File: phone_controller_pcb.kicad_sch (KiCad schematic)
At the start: 17 parts, among them J1 USB_C_Receptacle_USB2.0_14P, J3 Conn_01x05_Pin, J4 Conn_01x05_Pin, J5 Conn_01x05_Pin, SW1 SW_SPDT, U1 nRF52840, U2 USBLC6-2P6, Y1 ECS-320-8-37B-CKY-TR, Y2 ABS05-32.768KHZ-9-T

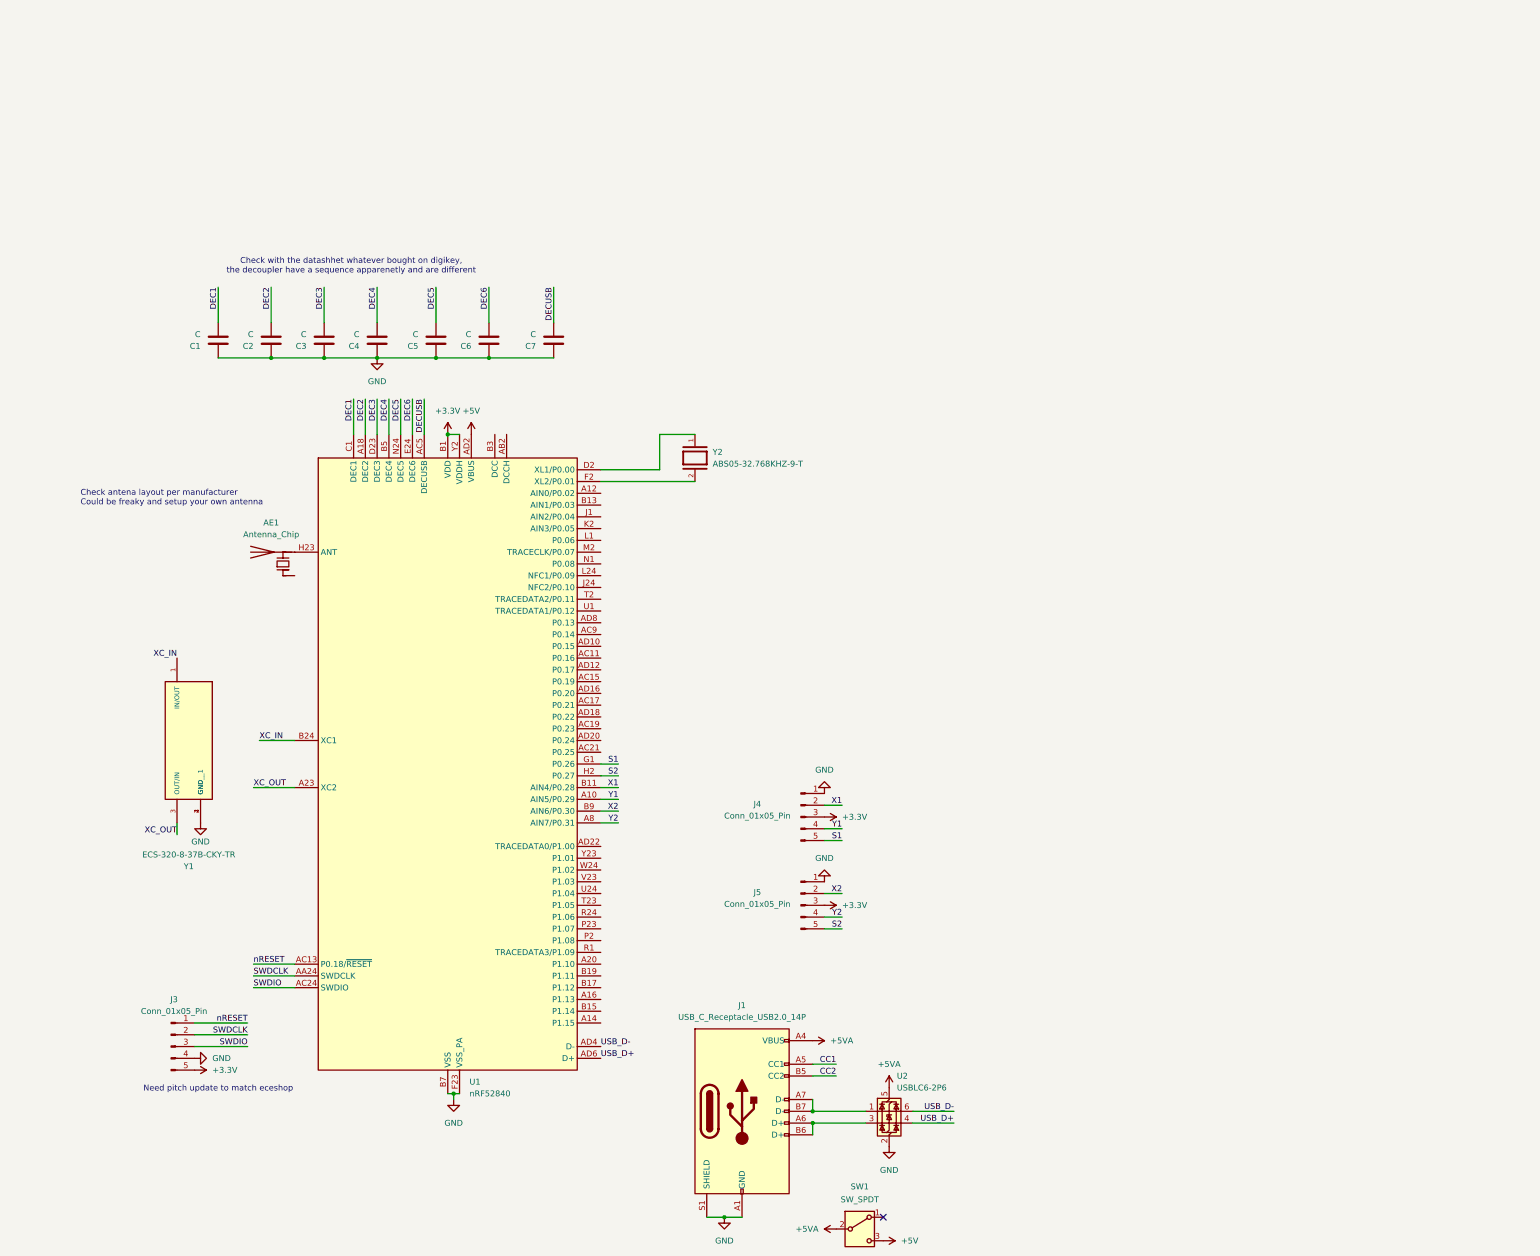
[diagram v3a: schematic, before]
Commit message: Added 3d model; update capacitor values
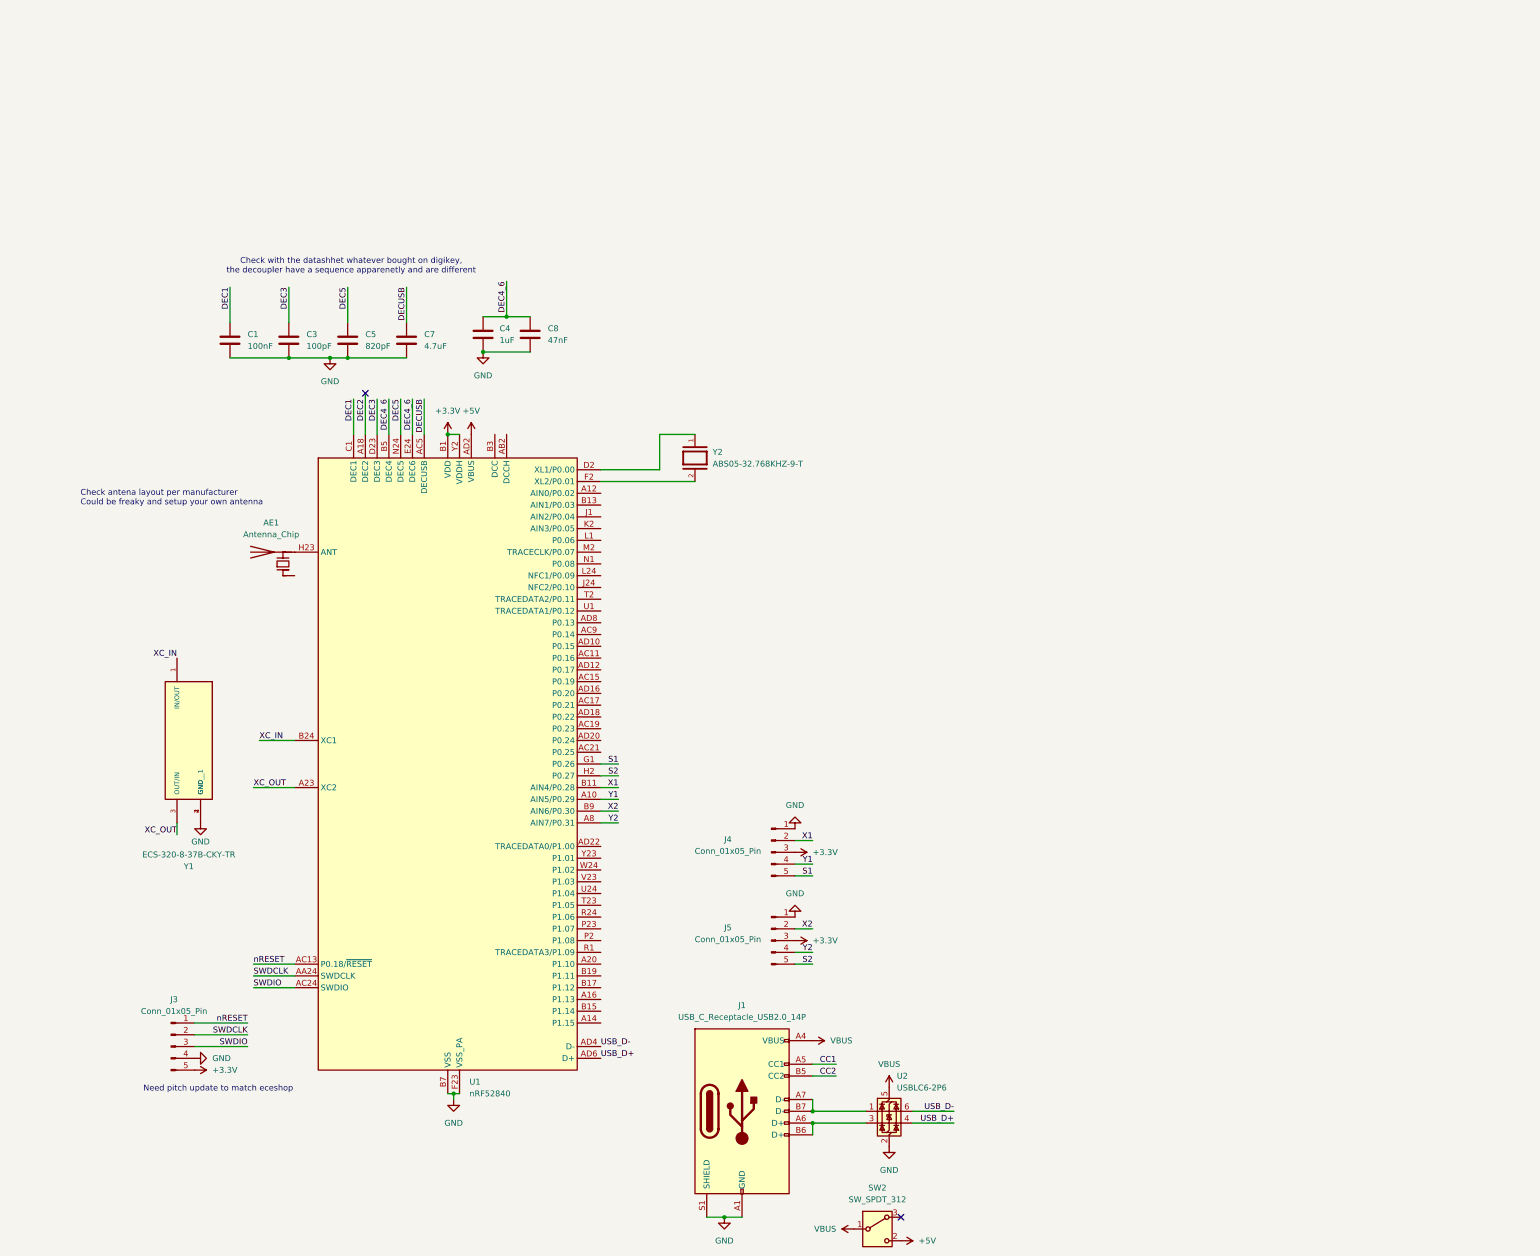
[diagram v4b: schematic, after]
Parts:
- removed C2, C6: C, Capacitor_SMD:C_0805_2012Metric, symbol Device:C
- removed SW1: SW_SPDT, symbol Switch:SW_SPDT
- added C8: 47nF, Capacitor_SMD:C_0805_2012Metric, symbol Device:C
- added SW2: SW_SPDT_312, footprints:OS102011MA1QN1_CNK, symbol Switch:SW_SPDT_312
- C1: value C -> 100nF
- C3: value C -> 100pF
- C4: value C -> 1uF
- C5: value C -> 820pF
- C7: value C -> 4.7uF
- J4, J5: footprint Connector_PinHeader_1.00mm:PinHeader_1x05_P1.00mm_Vertical -> 59453_052110ECHLF:AMPHENOL_59453-052110ECHLF; Digikey (none) -> https://www.digikey.com/en/products/detail/amphenol-icc-fci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
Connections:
- net DEC6 is gone; now on net DEC4_6: U1.E24 (DEC6)
- net +5V: now also SW2.2 (C)
- net GND: now also C8.2
- net +5VA renamed VBUS
- net VBUS: now also SW2.1 (B)
- net DEC4 renamed DEC4_6
- net DEC4_6: now also C8.1
- no-connect marks 1 -> 2
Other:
- moved on the sheet: C1, C3, C5, C7, J4, J5

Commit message: Added antenna setup; Added separator; Rounding out power capacitor
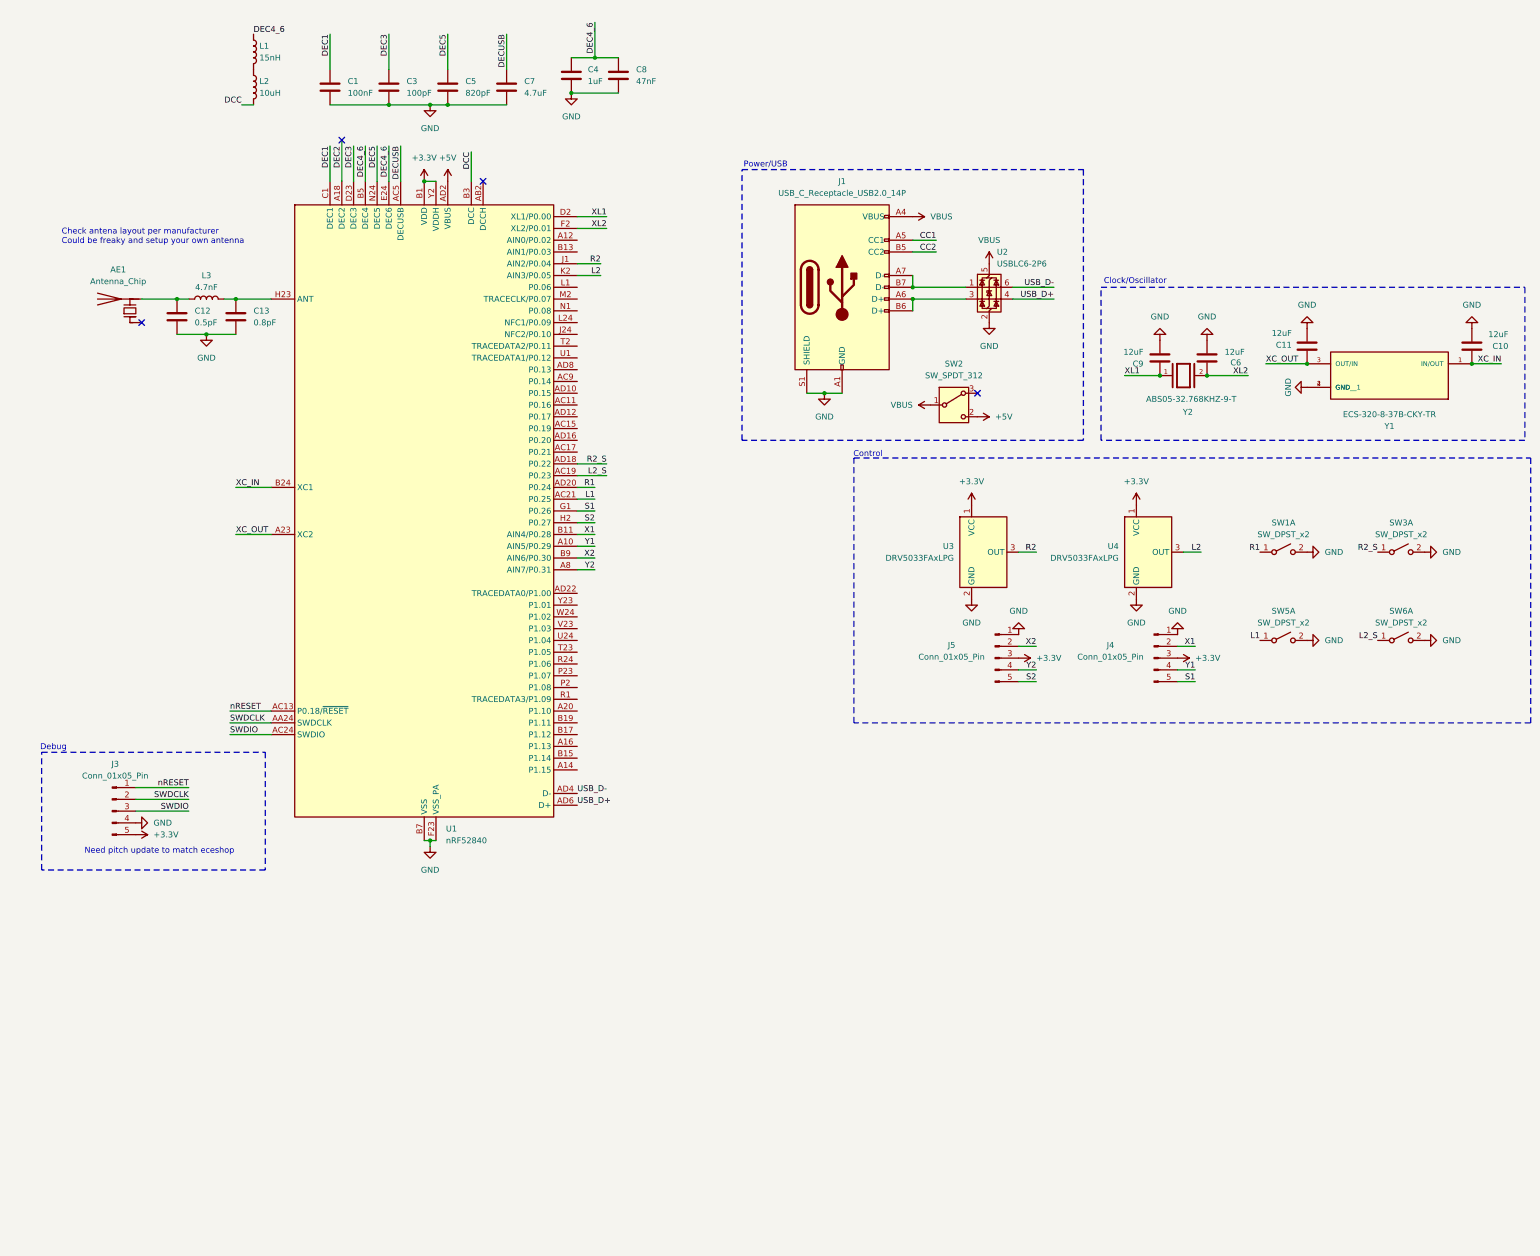
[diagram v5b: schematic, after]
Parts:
- added C10, C11, C6, C9: 12uF, Capacitor_SMD:C_0805_2012Metric, symbol Device:C
- added C12: 0.5pF, Capacitor_SMD:C_0805_2012Metric, symbol Device:C
- added C13: 0.8pF, Capacitor_SMD:C_0805_2012Metric, symbol Device:C
- added L1: 15nH, symbol Device:L
- added L2: 10uH, symbol Device:L
- added L3: 4.7nF, symbol Device:L
- added SW1, SW3, SW5, SW6: SW_DPST_x2, Button_Switch_THT:SW_NKK_GW12LJP, symbol Switch:SW_DPST_x2
- added U3, U4: DRV5033FAxLPG, Package_TO_SOT_THT:TO-92Flat, symbol Sensor_Magnetic:DRV5033FAxLPG
- AE1: Digikey (none) -> https://www.digikey.com/en/products/detail/abracon-llc/AMCA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
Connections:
- net +3.3V: now also U3.1 (VCC), U4.1 (VCC)
- net DEC4_6: now also L1.1
- net GND: now also C10.2, C11.2, C12.2, C13.2, C6.2, C9.2, SW1.2 (B), SW3.2 (B), SW5.2 (B), SW6.2 (B), U3.2 (GND), U4.2 (GND)
- net XC_IN: now also C10.1
- net XC_OUT: now also C11.1
- net at AE1.2 (PCB_Trace): now also C12.1, L3.1; no longer U1.H23 (ANT)
- net XL1: now reaches U1.D2 (XL1/P0.00), Y2.1
- net XL1: now also C9.1
- net XL2: now reaches U1.F2 (XL2/P0.01), Y2.2
- net XL2: now also C6.1
- net L2_S: now reaches U1.AC19 (P0.23)
- net L2_S: now also SW6.1 (A)
- net L1: now reaches U1.AC21 (P0.25)
- net L1: now also SW5.1 (A)
- net R2_S: now reaches U1.AD18 (P0.22)
- net R2_S: now also SW3.1 (A)
- net R1: now reaches U1.AD20 (P0.24)
- net R1: now also SW1.1 (A)
- net DCC: now reaches U1.B3 (DCC)
- net DCC: now also L2.2
- net R2: now reaches U1.J1 (AIN2/P0.04)
- net R2: now also U3.3 (OUT)
- net L2: now reaches U1.K2 (AIN3/P0.05)
- net L2: now also U4.3 (OUT)
- new net: C13.1, L3.2, U1.H23 (ANT)
- new net: L1.2, L2.1
- no-connect marks 2 -> 4
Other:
- note added: "Clock/Oscillator"
- note added: "Control"
- note added: "Debug"
- note added: "Power/USB"
- note removed: "Check with the datashhet whatever bought on digikey, the decoupler have a sequence apparenetly and are different"
- moved on the sheet: AE1, C1, C3, C4, C5, C7, C8, J1, J3, J4, J5, SW2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
